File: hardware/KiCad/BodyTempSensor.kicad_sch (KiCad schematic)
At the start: 83 parts, among them IC3 TMP117MAIDRVT, IC4 TMP117MAIDRVT, IC5 TMP117MAIDRVT, IC6 TMP117MAIDRVT, IC7 NRF54L15-QFAA-R, J1 USB_C_Receptacle_USB2.0, J3 BAT, J6 Conn_02x05_Odd_Even, Q1 NMOS, Q2 NMOS, U2 USBLC6-2SC6, U3 MCP73833-xxx-UN, U4 TLV62568DBVR, U5 MCP6001-OT, Y1 32MHz

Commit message: Did 80% of the PCB lay-out
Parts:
- removed U2: USBLC6-2SC6, Package_TO_SOT_SMD:SOT-23-6, symbol Power_Protection:USBLC6-2SC6
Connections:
- net USB_D+: no longer names the net of J1.A6 (D+)
- net USB_D+: no longer J1.B6 (D+)
- net USB_D-: no longer names the net of J1.A7 (D-)
- net USB_D-: no longer J1.B7 (D-)
- no-connect marks 15 -> 19
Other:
- note added: "MCU NRF54L15"
- note added: "NRF54L15-QFAA-R"
- note removed: "MCU NRF52840"
- note removed: "NRF52840-QIAA-F-R7"

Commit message: testing
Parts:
- added J2, J5: Conn_02x02_Odd_Even, Connector_PinHeader_1.27mm:PinHeader_2x02_P1.27mm_Vertical_SMD, symbol Connector_Generic:Conn_02x02_Odd_Even
- added J4, J7: Conn_02x02_Odd_Even, Connector_PinHeader_1.27mm:PinHeader_2x02_P1.27mm_Vertical, symbol Connector_Generic:Conn_02x02_Odd_Even
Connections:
- net +3V3: now also J2.1 (Pin_1), J4.1 (Pin_1), J5.1 (Pin_1), J7.1 (Pin_1)
- net Earth: now also J2.4 (Pin_4), J4.4 (Pin_4), J5.4 (Pin_4), J7.4 (Pin_4)
- net P0.17/SDA: now also J2.2 (Pin_2), J4.3 (Pin_3), J5.2 (Pin_2), J7.3 (Pin_3)
- net P0.19/SCL: now also J2.3 (Pin_3), J4.2 (Pin_2), J5.3 (Pin_3), J7.2 (Pin_2)
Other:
- moved on the sheet: C23, C25, IC4, IC6

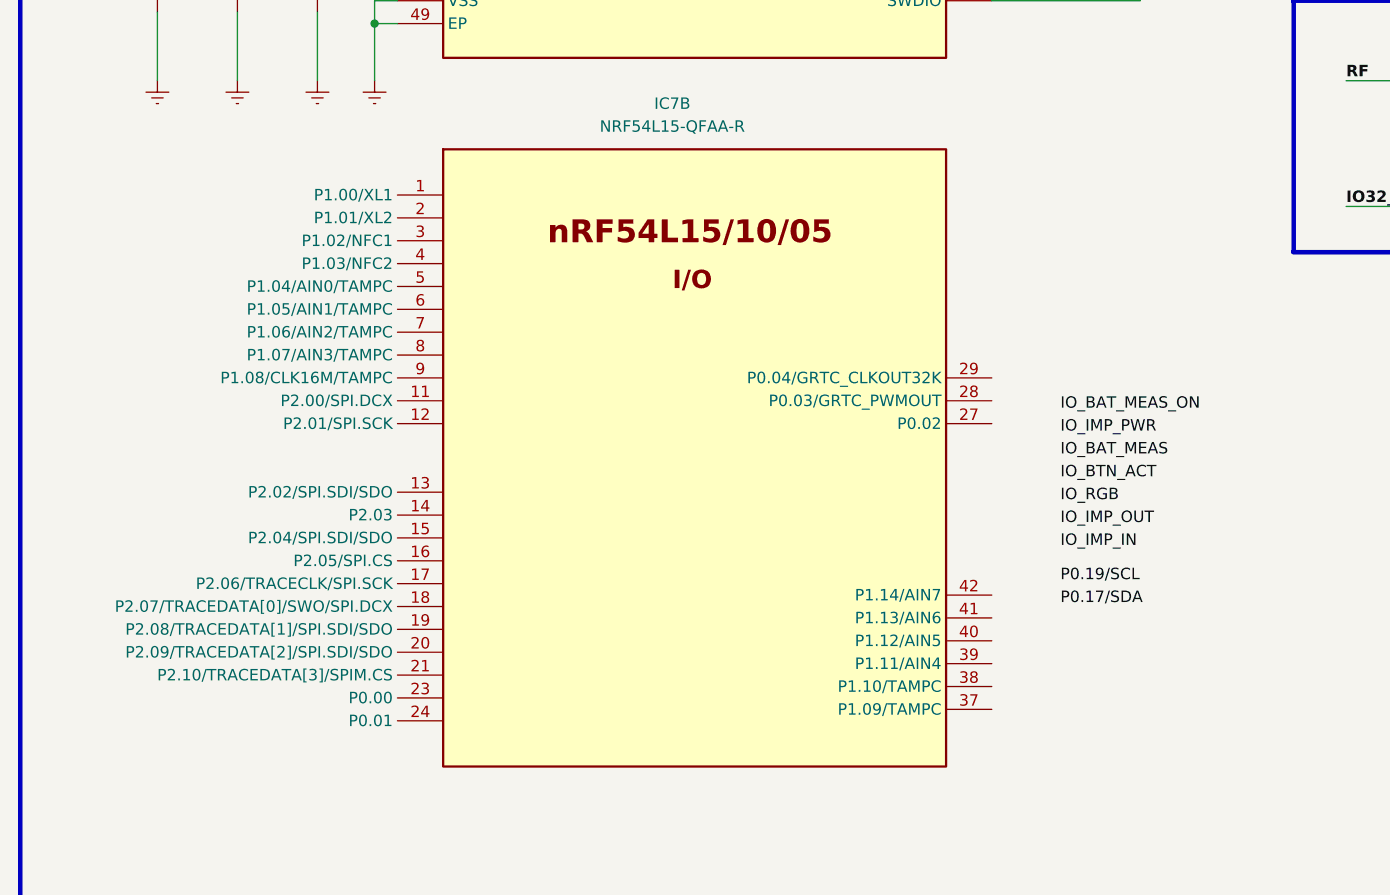
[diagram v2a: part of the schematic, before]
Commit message: Add new STEP files for KiCad and finalize the lay-out.
- Created new STEP file: Step3DBoard.step (5.1 MB)
- Created new STEP file: Unnamed1-Step3DBoard 1.step (7.8 MB)
- Added Excel data file: ~$BodyTempSens_Data.xlsx with initial data
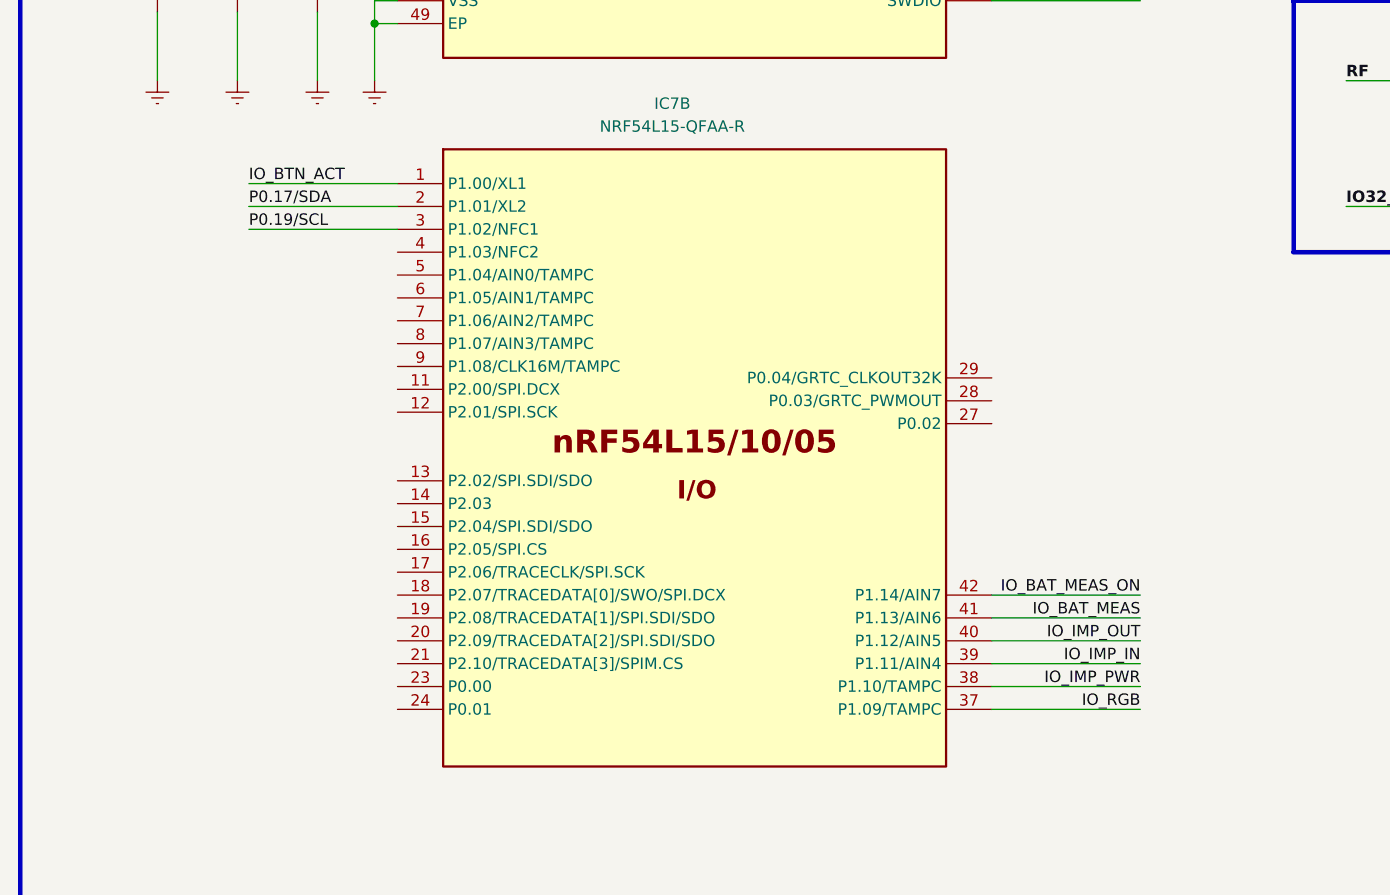
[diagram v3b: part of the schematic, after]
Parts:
- IC7: footprint PCB_Lib_ItsNotDaan:QFN40P600X600X95-49N -> LibLoader:QFN40P600X600X95-49N
- J3: footprint Connector_PinSocket_2.54mm:PinSocket_1x02_P2.54mm_Vertical -> Connector_JST:JST_PH_B2B-PH-K_1x02_P2.00mm_Vertical
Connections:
- net IO_BAT_MEAS: now also IC7.41 (P1.13/AIN6)
- net IO_BAT_MEAS_ON: now also IC7.42 (P1.14/AIN7)
- net IO_BTN_ACT: now also IC7.1 (P1.00/XL1)
- net IO_IMP_IN: now also IC7.39 (P1.11/AIN4)
- net IO_IMP_OUT: now also IC7.40 (P1.12/AIN5)
- net IO_IMP_PWR: now also IC7.38 (P1.10/TAMPC)
- net IO_RGB: now also IC7.37 (P1.09/TAMPC)
- net P0.17/SDA: now also IC7.2 (P1.01/XL2)
- net P0.19/SCL: now also IC7.3 (P1.02/NFC1)
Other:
- moved on the sheet: IC7B
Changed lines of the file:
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@@
 	(wire
 		(pts
+			(xy 137.16 275.59) (xy 120.65 275.59)
+		)
+		(stroke
+			(width 0)
+			(type default)
+		)
+	)
+	(wire
+		(pts
 			(xy 394.97 283.21) (xy 394.97 288.29)
 		)
@@
 	(wire
 		(pts
+			(xy 137.16 273.05) (xy 120.65 273.05)
+		)
+		(stroke
+			(width 0)
+			(type default)
+		)
+	)
+	(wire
+		(pts
 			(xy 375.92 172.72) (xy 375.92 176.53)
 		)
@@
 	(wire
 		(pts
+			(xy 38.1 229.87) (xy 54.61 229.87)
+		)
+		(stroke
+			(width 0)
+			(type default)
+		)
+	)
+	(wire
+		(pts
 			(xy 468.63 252.73) (xy 468.63 255.27)
 		)
@@
 	(wire
 		(pts
+			(xy 137.16 285.75) (xy 120.65 285.75)
+		)
+		(stroke
+			(width 0)
+			(type default)
+		)
+	)
+	(wire
+		(pts
 			(xy 199.39 57.15) (xy 204.47 57.15)
 		)
@@
 	(wire
 		(pts
+			(xy 38.1 232.41) (xy 54.61 232.41)
+		)
+		(stroke
+			(width 0)
+			(type default)
+		)
+	)
+	(wire
+		(pts
 			(xy 120.65 134.62) (xy 132.08 134.62)
 		)
@@
 	(wire
 		(pts
+			(xy 137.16 283.21) (xy 120.65 283.21)
+		)
+		(stroke
+			(width 0)
+			(type default)
+		)
+	)
+	(wire
+		(pts
 			(xy 264.16 184.15) (xy 264.16 186.69)
 		)
@@
 	(wire
 		(pts
+			(xy 38.1 227.33) (xy 54.61 227.33)
+		)
+		(stroke
+			(width 0)
+			(type default)
+		)
+	)
+	(wire
+		(pts
 			(xy 468.63 298.45) (xy 468.63 300.99)
 		)
@@
 	(wire
 		(pts
+			(xy 137.16 280.67) (xy 120.65 280.67)
+		)
+		(stroke
+			(width 0)
+			(type default)
+		)
+	)
+	(wire
+		(pts
 			(xy 195.58 257.81) (xy 195.58 255.27)
 		)
@@
 	(wire
 		(pts
+			(xy 137.16 278.13) (xy 120.65 278.13)
+		)
+		(stroke
+			(width 0)
+			(type default)
+		)
+	)
+	(wire
+		(pts
 			(xy 397.51 46.99) (xy 401.32 46.99)
 		)
@@
 	)
 	(label "P0.19/SCL"
-		(at 128.27 271.78 0)
+		(at 38.1 232.41 0)
 		(effects
 			(font
@@
 	)
 	(label "IO_IMP_IN"
-		(at 128.27 267.97 0)
+		(at 137.16 280.67 180)
 		(effects
 			(font
 				(size 1.27 1.27)
 			)
-			(justify left bottom)
+			(justify right bottom)
 		)
 	)
@@
 	)
 	(label "IO_BAT_MEAS_ON"
-		(at 128.27 252.73 0)
+		(at 137.16 273.05 180)
 		(effects
 			(font
 				(size 1.27 1.27)
 			)
-			(justify left bottom)
+			(justify right bottom)
 		)
 	)
@@
 	)
 	(label "IO_IMP_PWR"
-		(at 128.27 255.27 0)
+		(at 137.16 283.21 180)
 		(effects
 			(font
 				(size 1.27 1.27)
 			)
-			(justify left bottom)
+			(justify right bottom)
 		)
 	)
@@
 	)
 	(label "IO_RGB"
-		(at 128.27 262.89 0)
+		(at 137.16 285.75 180)
 		(effects
 			(font
 				(size 1.27 1.27)
 			)
-			(justify left bottom)
+			(justify right bottom)
 		)
 	)
 	(label "P0.17/SDA"
-		(at 128.27 274.32 0)
+		(at 38.1 229.87 0)
 		(effects
 			(font
@@
 	)
 	(label "IO_BTN_ACT"
-		(at 128.27 260.35 0)
+		(at 38.1 227.33 0)
 		(effects
 			(font
@@
 	)
 	(label "IO_BAT_MEAS"
-		(at 128.27 257.81 0)
+		(at 137.16 275.59 180)
 		(effects
 			(font
 				(size 1.27 1.27)
 			)
-			(justify left bottom)
+			(justify right bottom)
 		)
 	)
@@
 	)
 	(label "IO_IMP_OUT"
-		(at 128.27 265.43 0)
+		(at 137.16 278.13 180)
 		(effects
 			(font
 				(size 1.27 1.27)
 			)
-			(justify left bottom)
+			(justify right bottom)
 		)
 	)
@@
 	)
 	(symbol
+		(lib_name "NRF54L15-QFAA-R_1")
 		(lib_id "LibLoader:NRF54L15-QFAA-R")
 		(at 88.9 247.65 0)
@@
 			)
 		)
-		(property "Footprint" "PCB_Lib_ItsNotDaan:QFN40P600X600X95-49N"
+		(property "Footprint" "LibLoader:QFN40P600X600X95-49N"
 			(at 151.13 324.79 0)
 			(hide yes)
@@
 			)
 		)
-		(property "Description" "2.4GHz BLE/Thread/Zigbee SoC QFN-48 1.5MB NVM"
+		(property "Description" "RF System on a Chip - SoC Ultra-low power Bluetooth Multiprotocol 5.4 SoC System-on-Chip"
 			(at 88.9 247.65 0)
 			(hide yes)
@@
 			)
 		)
-		(property "Footprint" "Connector_PinSocket_2.54mm:PinSocket_1x02_P2.54mm_Vertical"
+		(property "Footprint" "Connector_JST:JST_PH_B2B-PH-K_1x02_P2.00mm_Vertical"
 			(at 254 54.61 0)
 			(hide yes)
